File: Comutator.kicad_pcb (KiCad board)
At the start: 2 copper layers, 11 parts, among them J2 Conn_01x02, K1 G5V-2, Q1 IRLML2402, Q2 IRLML2402, Q3 BT139-600

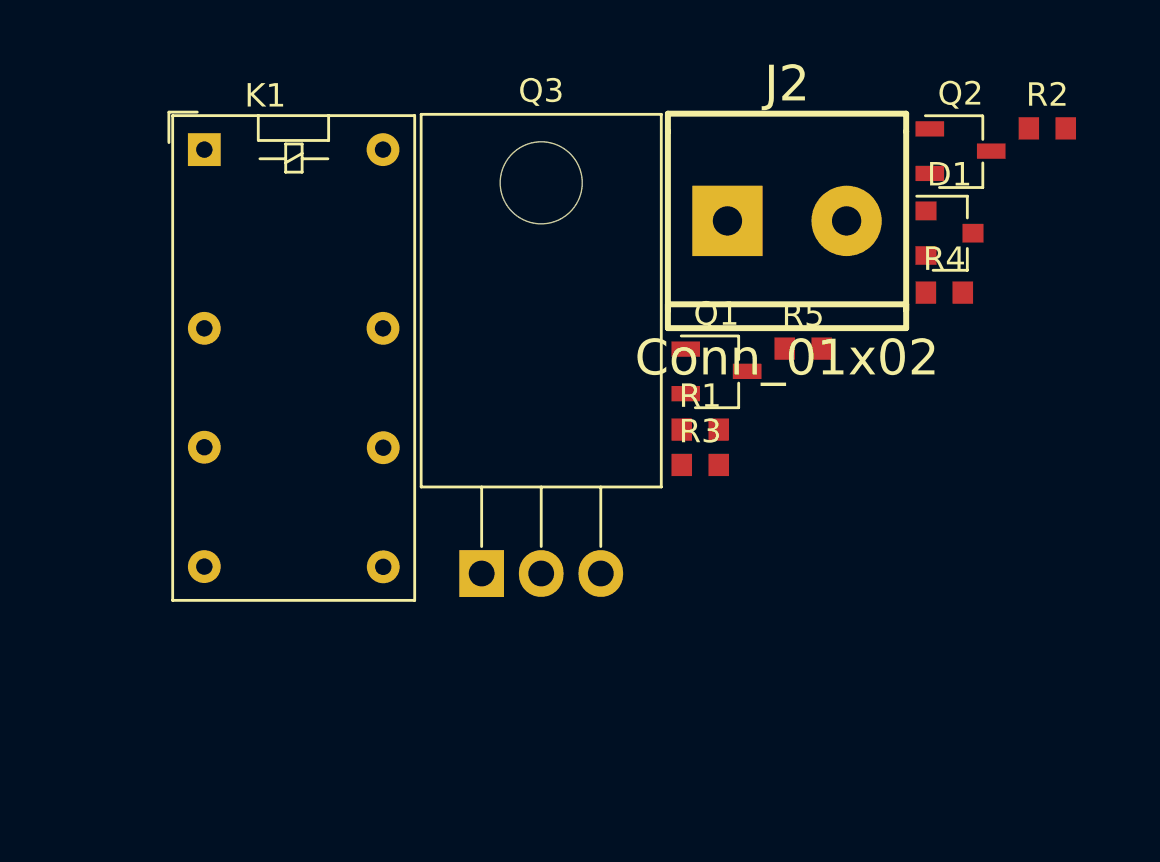
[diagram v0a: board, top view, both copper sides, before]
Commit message: Add SO-6 package
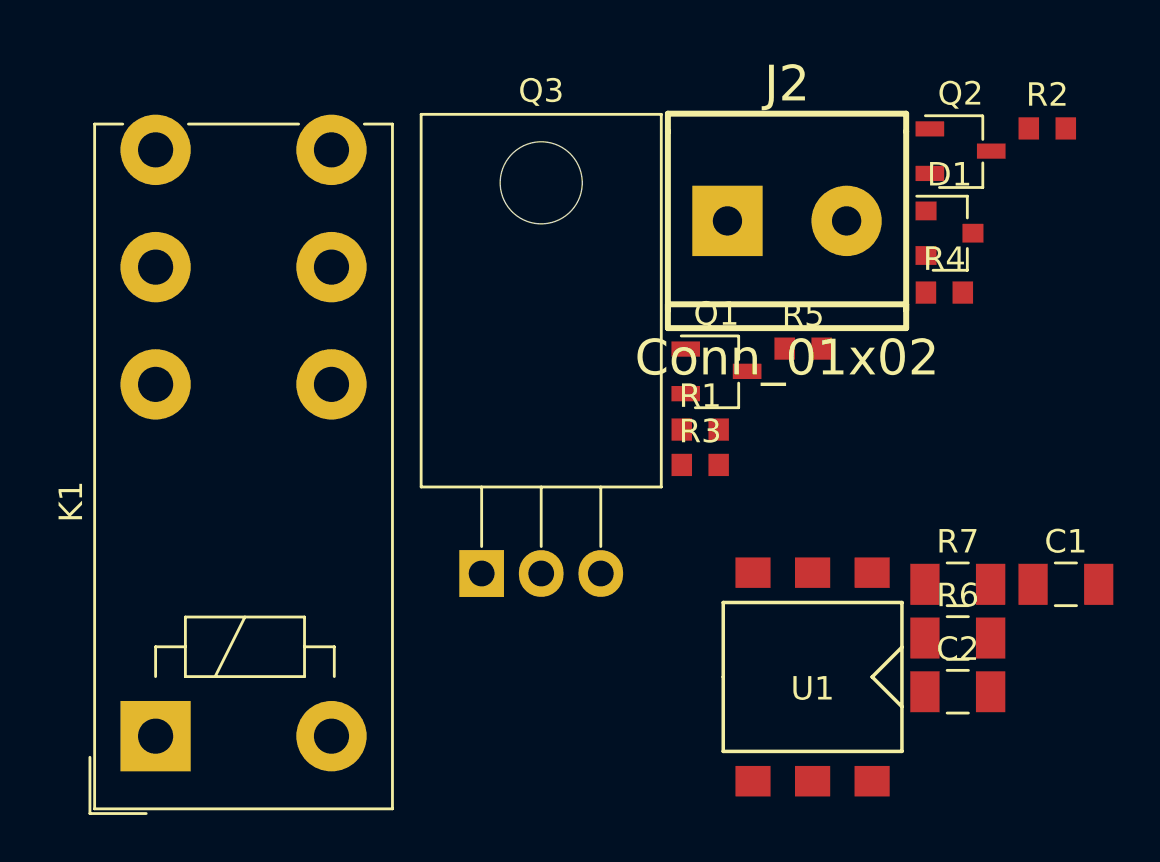
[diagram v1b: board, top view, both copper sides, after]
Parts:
- added C1: 1u, Capacitor_SMD:C_1206_3216Metric, F.Cu at (163.3, 101.5)
- added C2: 1u, Capacitor_SMD:C_1206_3216Metric, F.Cu at (158.7, 106.1)
- added R6: 360, Resistor_SMD:R_1206_3216Metric, F.Cu at (158.7, 103.8)
- added R7: 360, Resistor_SMD:R_1206_3216Metric, F.Cu at (158.7, 101.5)
- added U1: MOC3063M, comutator:SO-6, F.Cu at (152.5, 105.4)
- K1: value G5V-2 -> FINDER-40.52; footprint Relay_THT:Relay_DPDT_Omron_G5V-2 -> Relay_THT:Relay_DPDT_Finder_40.52
- moved K1 25.1 mm to (124.5, 108.0), turned to 90 degrees
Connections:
- K1 pad 11: Net-(K1-Pad11) -> Net-(J2-Pad1)

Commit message: Create pcb
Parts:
- added D2: BZG05C9V1, Diode_SMD:D_MiniMELF, F.Cu at (173.5, 118.3)
- added D3: LED, LED_THT:LED_D3.0mm, B.Cu at (164.5, 117.5)
- added J1: Conn_01x03, Connector_PinHeader_2.54mm:PinHeader_1x03_P2.54mm_Vertical, B.Cu at (143.5, 111.1)
- C1, C2: footprint Capacitor_SMD:C_1206_3216Metric -> Capacitor_SMD:C_0805_2012Metric
- J2, K1: moved to B.Cu
- R1, R2, R3, R4, R5: footprint Resistor_SMD:R_0603_1608Metric -> Resistor_SMD:R_0805_2012Metric
- U1: footprint comutator:SO-6 -> Package_DIP:DIP-6_W7.62mm; moved to B.Cu
- moved K1 64.1 mm to (188.0, 116.6)
- moved Q3 35.7 mm to (172.7, 91.4), turned to 180 degrees
- moved J2 34.4 mm to (185.4, 81.3), turned to 90 degrees
- moved R7 29.2 mm to (170.3, 74.7), turned to 180 degrees
- moved R4 28.5 mm to (159.8, 117.5), turned to 180 degrees
- moved R6 27.6 mm to (170.3, 78.7), turned to 180 degrees
- moved U1 22.0 mm to (156.5, 83.8)
- moved C2 21.4 mm to (144.4, 90.2), turned to 180 degrees
- moved R2 21.2 mm to (149.3, 98.6)
- moved C1 19.1 mm to (144.4, 98.6), turned to 180 degrees
- moved R1 13.9 mm to (148.4, 108.7), turned to 180 degrees
- moved Q1 12.7 mm to (149.4, 105.1)
- moved R5 12.7 mm to (151.6, 78.7)
- moved D1 12.1 mm to (149.1, 94.3)
- moved Q2 7.78 mm to (151.1, 84.1)
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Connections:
- K1 pad 11: Net-(J2-Pad1) -> Net-(J2-Pad2)
- K1 pad 14: Net-(J2-Pad2) -> Net-(J2-Pad1)
- K1 pad 21: Net-(J2-Pad1) -> Net-(J2-Pad2)
- K1 pad 24: Net-(J2-Pad2) -> Net-(J2-Pad1)
- Q3 pad 1: Net-(J2-Pad2) -> Net-(J2-Pad1)
- Q3 pad 2: Net-(J2-Pad1) -> Net-(J2-Pad2)
- R6 pad 1: Net-(J2-Pad1) -> Net-(J2-Pad2)
- R7 pad 1: Net-(J2-Pad2) -> Net-(J2-Pad1)
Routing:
- net +5V: track 0.00 -> 97.9 mm
- net Net-(J2-Pad1): track 0.00 -> 52.2 mm
- net Net-(J2-Pad2): track 0.00 -> 51.3 mm
- net Net-(D2-Pad2): track 0.00 -> 39.5 mm
- net GND: track 0.00 -> 30.8 mm
- net Net-(Q3-Pad3): track 0.00 -> 27.5 mm
- net Net-(C2-Pad1): track 0.00 -> 19.0 mm
- net Net-(D1-Pad3): track 0.00 -> 18.9 mm
- net Net-(R5-Pad2): track 0.00 -> 16.9 mm
- net Net-(C1-Pad1): track 0.00 -> 16.2 mm
- net Net-(R6-Pad2): track 0.00 -> 8.94 mm
- net Net-(K1-Pad12): track 0.00 -> 7.50 mm
- net Net-(Q2-Pad3): track 0.00 -> 5.92 mm
- net Net-(J1-Pad2): track 0.00 -> 4.12 mm
- net Net-(D3-Pad1): track 0.00 -> 3.81 mm
- added copper zone on F.Cu, net Net-(J2-Pad2)
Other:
- board outline added: 55 x 50 mm
- net class +5V added: clearance 0.2, trace_width 0.5, via_dia 0.8, via_drill 0.4
